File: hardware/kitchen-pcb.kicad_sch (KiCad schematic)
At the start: 44 parts, among them J1 MEM2075-00-140-01-A, J2 Conn_02x02_Odd_Even, J3 Conn_01x06, J4 S3B-XH-SM4-TB_LF__SN_, Q1 TEMT6000X01, U1 SHT30-DIS-B, U2 MX25L3233FM2I-08G

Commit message: Error, warning free routing v0.1 (no silkscreen)
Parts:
- TP1, TP2, TP3, TP4, TP5: footprint TestPoint:TestPoint_Pad_D2.0mm -> TestPoint:TestPoint_Pad_D1.0mm
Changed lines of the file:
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@@
 			)
 		)
-		(property "Footprint" "TestPoint:TestPoint_Pad_D2.0mm"
+		(property "Footprint" "TestPoint:TestPoint_Pad_D1.0mm"
 			(at 123.19 182.88 0)
 			(effects
@@
 			)
 		)
-		(property "Footprint" "TestPoint:TestPoint_Pad_D2.0mm"
+		(property "Footprint" "TestPoint:TestPoint_Pad_D1.0mm"
 			(at 123.19 157.48 0)
 			(effects
@@
 			)
 		)
-		(property "Footprint" "TestPoint:TestPoint_Pad_D2.0mm"
+		(property "Footprint" "TestPoint:TestPoint_Pad_D1.0mm"
 			(at 123.19 176.53 0)
 			(effects
@@
 			)
 		)
-		(property "Footprint" "TestPoint:TestPoint_Pad_D2.0mm"
+		(property "Footprint" "TestPoint:TestPoint_Pad_D1.0mm"
 			(at 123.19 170.18 0)
 			(effects
@@
 			)
 		)
-		(property "Footprint" "TestPoint:TestPoint_Pad_D2.0mm"
+		(property "Footprint" "TestPoint:TestPoint_Pad_D1.0mm"
 			(at 123.19 163.83 0)
 			(effects

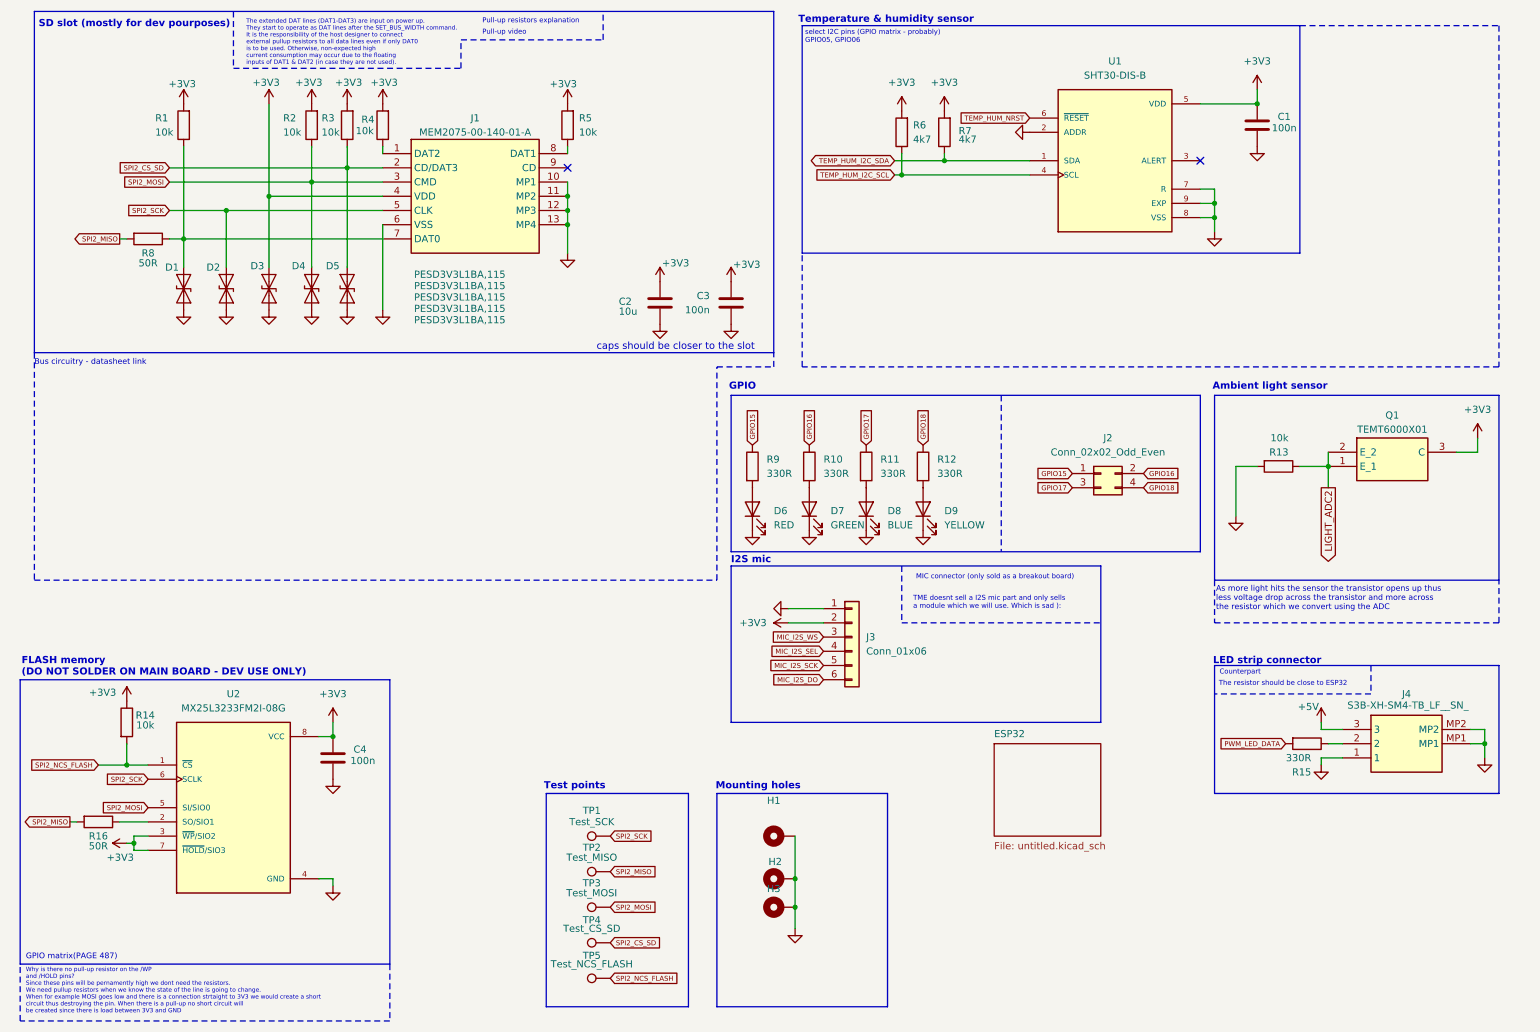
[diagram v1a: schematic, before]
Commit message: v0.3.1 Changed board stackup and impedance controlled traces
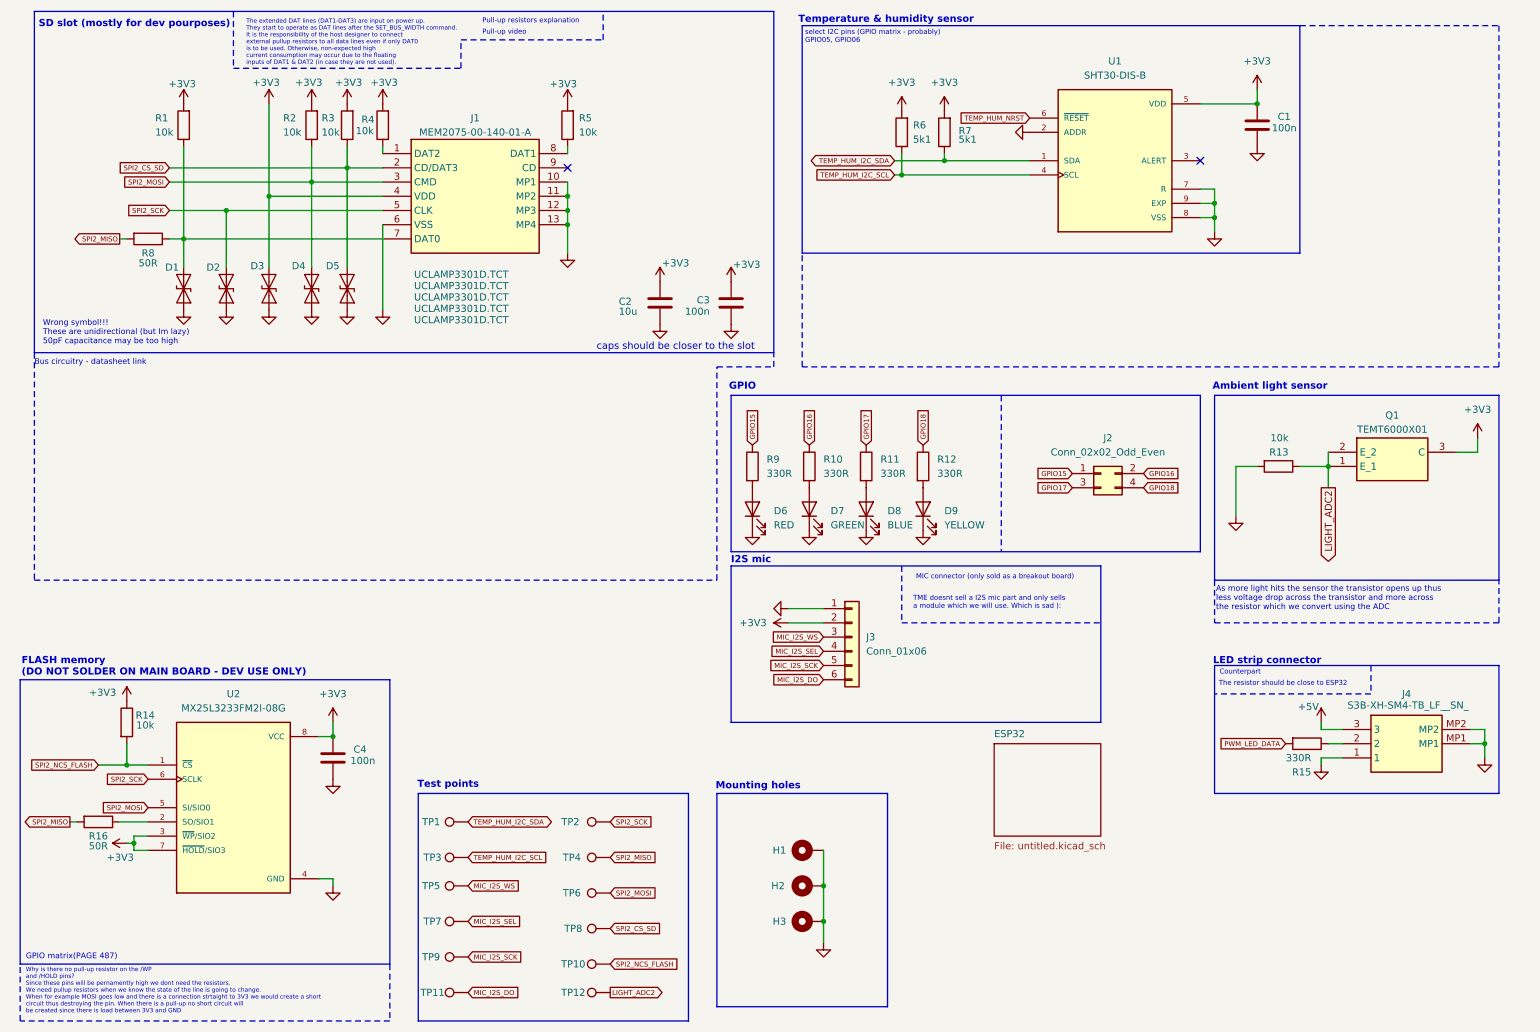
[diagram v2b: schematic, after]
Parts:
- added TP1, TP5: Test_SCK, TestPoint:TestPoint_Pad_D1.0mm, symbol Connector:TestPoint
- added TP11: Test_CS_SD, TestPoint:TestPoint_Pad_D1.0mm, symbol Connector:TestPoint
- added TP12: Test_NCS_FLASH, TestPoint:TestPoint_Pad_D1.0mm, symbol Connector:TestPoint
- added TP3, TP7: Test_MISO, TestPoint:TestPoint_Pad_D1.0mm, symbol Connector:TestPoint
- added TP9: Test_MOSI, TestPoint:TestPoint_Pad_D1.0mm, symbol Connector:TestPoint
- D1, D2, D3, D4, D5: value PESD3V3L1BA,115 -> UCLAMP3301D.TCT
- R6, R7: value 4k7 -> 5k1; footprint Resistor_SMD:R_0603_1608Metric_Pad0.98x0.95mm_HandSolder -> Resistor_SMD:R_0805_2012Metric_Pad1.20x1.40mm_HandSolder
- renumbered TP5 to TP10, TP1 to TP2, TP2 to TP4, TP3 to TP6, TP4 to TP8
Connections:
- net LIGHT_ADC2: now also TP12.1
- net MIC_I2S_DO: now also TP11.1
- net MIC_I2S_SCK: now also TP9.1
- net MIC_I2S_SEL: now also TP7.1
- net MIC_I2S_WS: now also TP5.1
- net TEMP_HUM_I2C_SCL: now also TP3.1
- net TEMP_HUM_I2C_SDA: now also TP1.1
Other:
- note added: "Wrong symbol!!! These are unidirectional (but Im lazy) 50pF capacitance may be too high"
- moved on the sheet: H1, H2, H3, TP10, TP2, TP4, TP6, TP8
